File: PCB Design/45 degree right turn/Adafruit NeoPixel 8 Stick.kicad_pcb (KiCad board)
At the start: 2 copper layers, 26 x 21.4 mm, 4 parts, among them CN1 1X4SMT, CN2 1X4SMT

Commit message: arrows
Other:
- board text removed: "DIN"
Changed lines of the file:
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@@
       (net 2 "GND") (pinfunction "4") (pintype "bidirectional") (solder_mask_margin 0.1016))
   )
+  (gr_line (start 137.668 109.22) (end 134.874 110.236) (layer "B.SilkS") (width 0.12))
+  (gr_line (start 137.668 109.22) (end 136.652 106.68) (layer "B.SilkS") (width 0.12))
+  (gr_line (start 129.794 106.172) (end 137.668 109.22) (layer "B.SilkS") (width 0.12))
   (gr_line (start 131.064 113.792) (end 122.428 113.792) (layer "Edge.Cuts") (width 0.05))
   (gr_line (start 137.272687 119.934677) (end 131.166113 113.828103) (layer "Edge.Cuts") (width 0.05))
@@
     (effects (font (size 1.143 1.143) (thickness 0.127)) (justify left bottom mirror))
   )
-  (gr_text "4-7VDC" (at 128.9812 107.0864) (layer "B.SilkS")
-    (effects (font (size 1.143 1.143) (thickness 0.127)) (justify right top mirror))
-  )
   (gr_text "DOUT" (at 155.194 131.4704 270) (layer "B.SilkS")
     (effects (font (size 1.143 1.143) (thickness 0.127)) (justify left bottom mirror))
@@
     (effects (font (size 1.143 1.143) (thickness 0.127)) (justify left bottom mirror))
   )
-  (gr_text "DIN" (at 128.9812 105.0544) (layer "B.SilkS")
-    (effects (font (size 1.143 1.143) (thickness 0.127)) (justify right top mirror))
-  )
   (gr_text "GND" (at 157.734 131.4704 270) (layer "B.SilkS")
     (effects (font (size 1.143 1.143) (thickness 0.127)) (justify left bottom mirror))
   )
-  (gr_text "GND" (at 128.9812 102.5144) (layer "B.SilkS")
-    (effects (font (size 1.143 1.143) (thickness 0.127)) (justify right top mirror))
-  )
-  (gr_text "GND" (at 128.9812 109.1184) (layer "B.SilkS")
-    (effects (font (size 1.143 1.143) (thickness 0.127)) (justify right top mirror))
-  )
   (segment (start 135.705782 112.591782) (end 138.360218 112.591782) (width 0.25) (layer "F.Cu") (net 1))

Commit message: 6 pin
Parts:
- moved CN1 2.67 mm to (139.4, 113.6)
- moved D2 2.34 mm to (138.4, 112.0)
- moved D1 1.70 mm to (128.8, 108.0)
- moved CN2 0.52 mm to (126.9, 107.4)
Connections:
- CN1 pad 1: GND -> Net-(CN1-Pad1)
- CN1 pad 2: Net-(D2-Pad2) -> Net-(CN1-Pad2)
- CN1 pad 3: +5V -> GND
- CN1 pad 4: GND -> Net-(CN1-Pad4)
- D2 pad 2: Net-(D2-Pad2) -> Net-(CN1-Pad4)
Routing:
- net Net-(CN1-Pad1): track 0.00 -> 22.6 mm
- net Net-(CN1-Pad2): track 0.00 -> 20.1 mm
- net +5V: track 13.3 -> 19.7 mm
- net Net-(CN2-Pad3): track 3.94 -> 0.00 mm
- net Net-(CN1-Pad4): track 0.00 -> 3.66 mm, vias 0 -> 1
- net Net-(D1-Pad2): track 5.57 -> 6.86 mm
- net Net-(D2-Pad2): vias 1 -> 0
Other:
- board size 26 x 21.4 mm -> 27.9 x 26.4 mm
- board text removed: "4-7VDC"
- board text removed: "DOUT"
- board text removed: "GND"

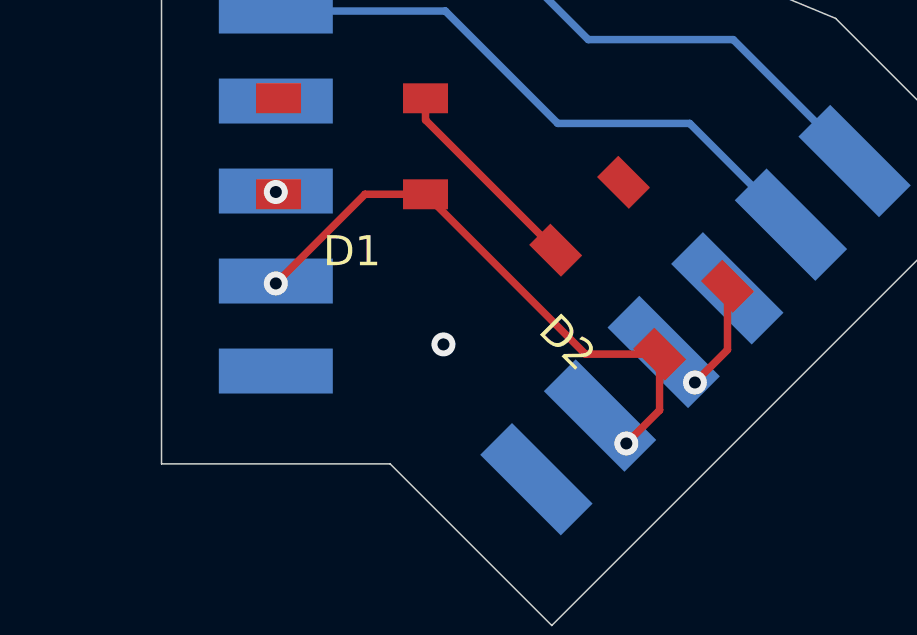
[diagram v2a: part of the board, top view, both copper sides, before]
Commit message: move vias off pads
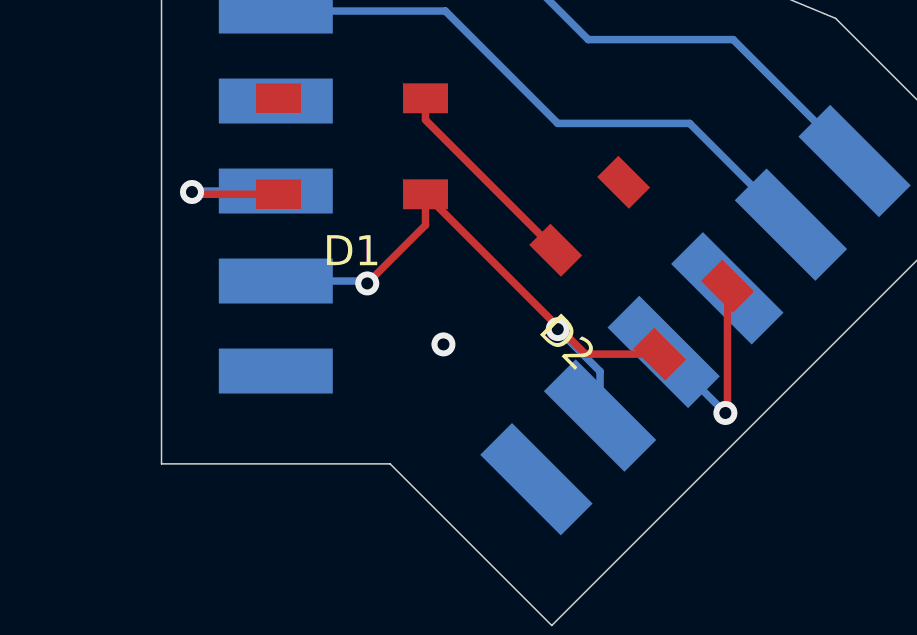
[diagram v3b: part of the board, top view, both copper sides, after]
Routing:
- net Net-(CN2-Pad3): track 0.00 -> 5.72 mm
- net Net-(CN1-Pad4): track 3.66 -> 7.15 mm
- net +5V: track 19.7 -> 20.3 mm
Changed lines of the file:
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@@
   (gr_line (start 122.428 97.536) (end 130.048 97.536) (layer "Edge.Cuts") (width 0.05))
   (segment (start 131.228 109.55) (end 136.555782 114.877782) (width 0.25) (layer "F.Cu") (net 1))
-  (segment (start 139.031041 116.746959) (end 139.031041 114.877782) (width 0.25) (layer "F.Cu") (net 1))
-  (segment (start 126.238 112.522) (end 129.21 109.55) (width 0.25) (layer "F.Cu") (net 1))
-  (segment (start 137.922 117.856) (end 139.031041 116.746959) (width 0.25) (layer "F.Cu") (net 1))
+  (segment (start 129.286 112.522) (end 131.228 110.58) (width 0.25) (layer "F.Cu") (net 1))
+  (segment (start 131.228 110.58) (end 131.228 109.55) (width 0.25) (layer "F.Cu") (net 1))
   (segment (start 136.555782 114.877782) (end 139.031041 114.877782) (width 0.25) (layer "F.Cu") (net 1))
-  (segment (start 129.21 109.55) (end 131.228 109.55) (width 0.25) (layer "F.Cu") (net 1))
-  (via (at 126.238 112.522) (size 0.8) (drill 0.4) (layers "F.Cu" "B.Cu") (net 1))
-  (via (at 137.922 117.856) (size 0.8) (drill 0.4) (layers "F.Cu" "B.Cu") (net 1))
+  (via (at 129.286 112.522) (size 0.8) (drill 0.4) (layers "F.Cu" "B.Cu") (net 1))
+  (via (at 135.636 114.046) (size 0.8) (drill 0.4) (layers "F.Cu" "B.Cu") (net 1))
+  (segment (start 137.045535 115.455535) (end 137.045535 116.926628) (width 0.25) (layer "B.Cu") (net 1))
+  (segment (start 126.238 112.442) (end 129.206 112.442) (width 0.25) (layer "B.Cu") (net 1))
+  (segment (start 129.206 112.442) (end 129.286 112.522) (width 0.25) (layer "B.Cu") (net 1))
+  (segment (start 135.636 114.046) (end 137.045535 115.455535) (width 0.25) (layer "B.Cu") (net 1))
   (via (at 131.826 114.554) (size 0.8) (drill 0.4) (layers "F.Cu" "B.Cu") (free) (net 2))
   (segment (start 135.636 107.188) (end 140.034829 107.188) (width 0.25) (layer "B.Cu") (net 3))
@@
   (segment (start 131.89 103.442) (end 135.636 107.188) (width 0.25) (layer "B.Cu") (net 3))
   (segment (start 126.238 103.442) (end 131.89 103.442) (width 0.25) (layer "B.Cu") (net 3))
-  (via (at 126.238 109.474) (size 0.8) (drill 0.4) (layers "F.Cu" "B.Cu") (net 4))
+  (segment (start 123.444 109.474) (end 123.52 109.55) (width 0.25) (layer "F.Cu") (net 4))
+  (segment (start 123.52 109.55) (end 126.328 109.55) (width 0.25) (layer "F.Cu") (net 4))
+  (via (at 123.444 109.474) (size 0.8) (drill 0.4) (layers "F.Cu" "B.Cu") (net 4))
+  (segment (start 123.476 109.442) (end 126.238 109.442) (width 0.25) (layer "B.Cu") (net 4))
+  (segment (start 123.444 109.474) (end 123.476 109.442) (width 0.25) (layer "B.Cu") (net 4))
   (segment (start 131.228 106.35) (end 131.228 107.074741) (width 0.25) (layer "F.Cu") (net 5))
   (segment (start 131.228 107.074741) (end 135.566218 111.412959) (width 0.25) (layer "F.Cu") (net 5))
@@
   (segment (start 136.652 104.394) (end 141.483469 104.394) (width 0.25) (layer "B.Cu") (net 6))
   (segment (start 132.7 100.442) (end 136.652 104.394) (width 0.25) (layer "B.Cu") (net 6))
-  (segment (start 141.293782 114.738218) (end 140.208 115.824) (width 0.25) (layer "F.Cu") (net 7))
-  (segment (start 141.293782 112.615041) (end 141.293782 114.738218) (width 0.25) (layer "F.Cu") (net 7))
-  (via (at 140.208 115.824) (size 0.8) (drill 0.4) (layers "F.Cu" "B.Cu") (net 7))
+  (segment (start 141.293782 112.615041) (end 141.293782 116.770218) (width 0.25) (layer "F.Cu") (net 7))
+  (segment (start 141.293782 116.770218) (end 141.224 116.84) (width 0.25) (layer "F.Cu") (net 7))
+  (via (at 141.224 116.84) (size 0.8) (drill 0.4) (layers "F.Cu" "B.Cu") (net 7))
+  (segment (start 139.166855 114.805308) (end 139.189308 114.805308) (width 0.25) (layer "B.Cu") (net 7))
+  (segment (start 139.189308 114.805308) (end 141.224 116.84) (width 0.25) (layer "B.Cu") (net 7))
   (zone (net 2) (net_name "GND") (layers F&B.Cu) (hatch edge 0.508)
     (priority 6)
